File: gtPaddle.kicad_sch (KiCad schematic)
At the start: 36 parts, among them IC1 74157N, IC2 74157N, J1 Conn_01x02_Pin, J2 Conn_01x02_Pin, J3 Conn_01x02_Pin, J4 Conn_01x02_Pin, Q1 2N3904, U1 ADC0804LCN

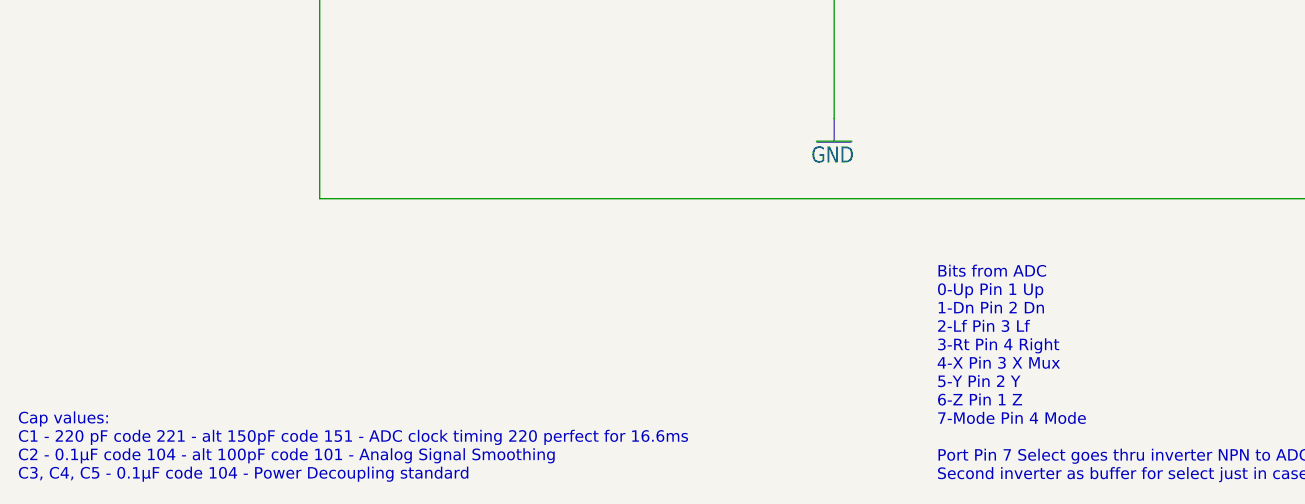
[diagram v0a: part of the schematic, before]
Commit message: added notes on resistor values
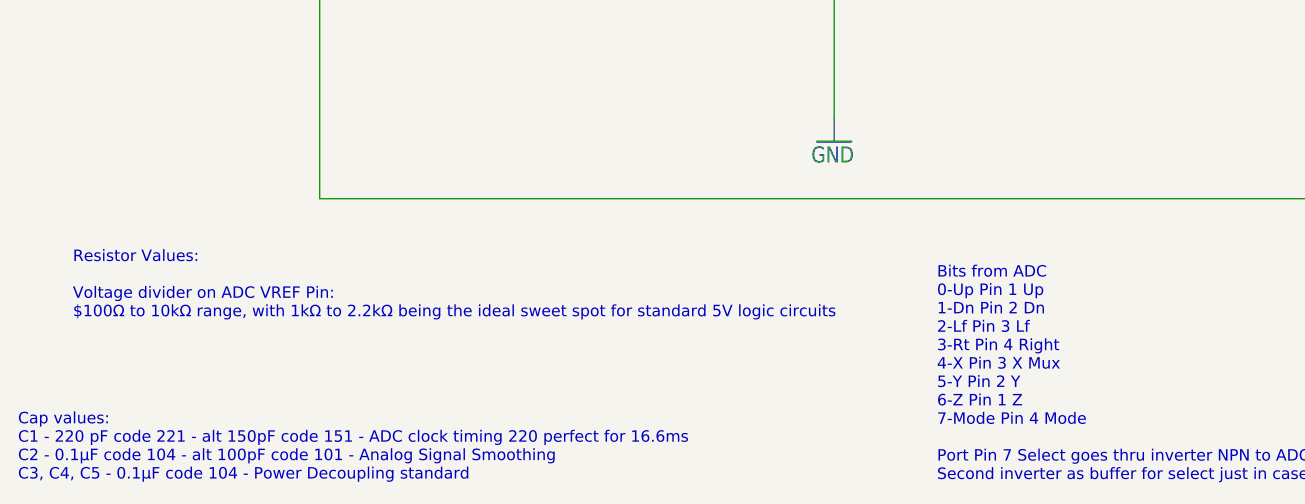
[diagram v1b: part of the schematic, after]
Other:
- note added: "Resistor Values: Voltage divider on ADC VREF Pin: $100Ω to 10kΩ range, with 1kΩ to 2.2kΩ being the ideal sweet spot for standard 5V logic circuits"
